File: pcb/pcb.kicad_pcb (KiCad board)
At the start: 2 copper layers, 43.2 x 132.1 mm, 49 parts, among them J1 Barrel_Jack_Switch, J2 Conn_02x05_Odd_Even, J3 Conn_02x05_Odd_Even, Q1 RQ5P010SN, Q2 IRLML6244, SW1 SW_SPST, SW2 SW_SPST, SW3 SW_SPST, U1 L7805, U2 MCP1406/07, U3 MAX6921AWI, U4 MCP7940N-xSN, U5 Pico, Y1 32.768KHZ

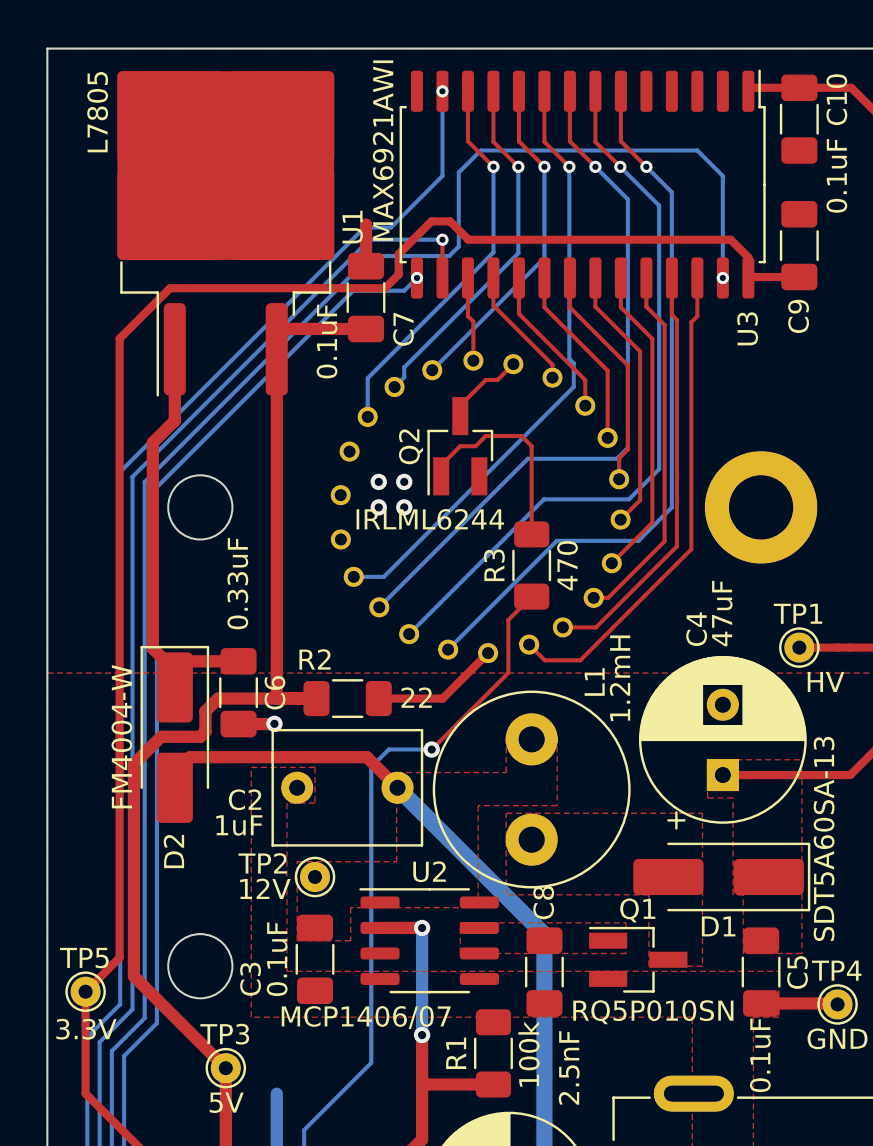
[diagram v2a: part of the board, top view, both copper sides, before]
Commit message: exchanged lm7805 for vx7805
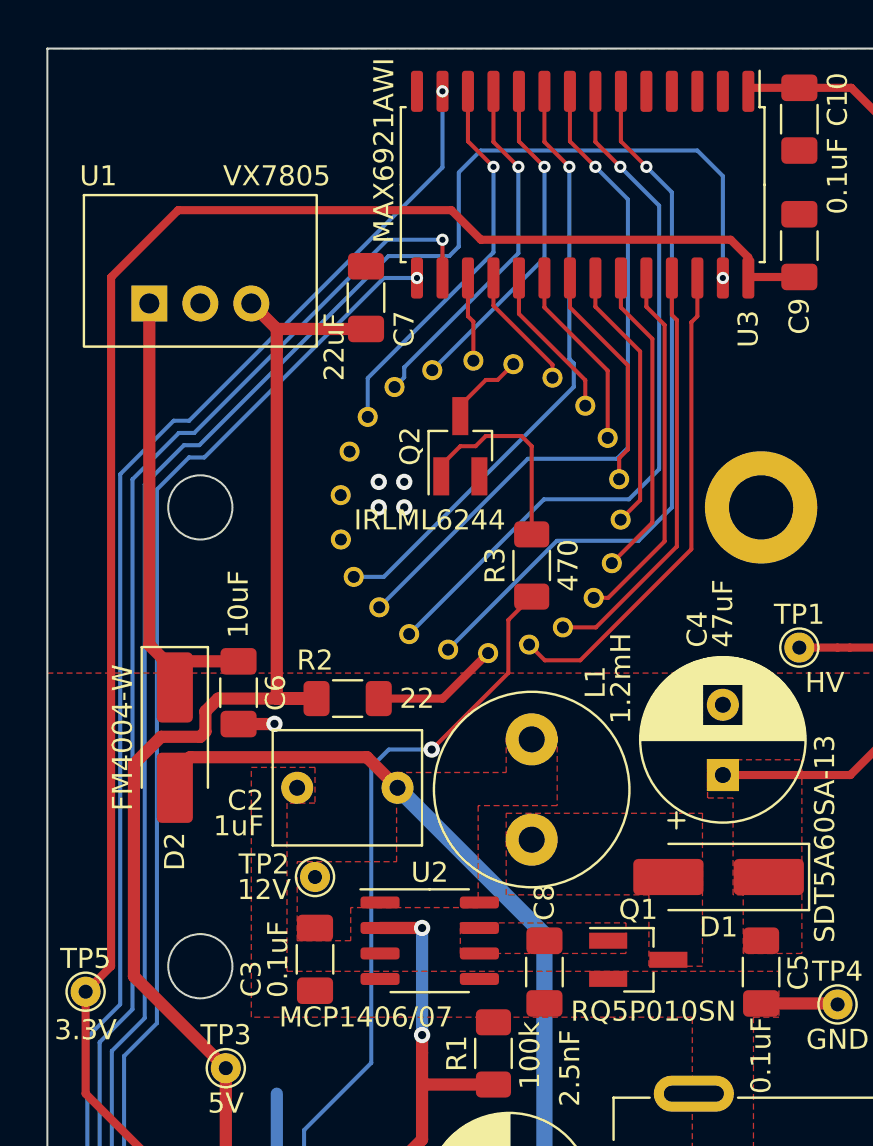
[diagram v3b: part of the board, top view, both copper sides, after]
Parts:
- C6: value 0.33uF -> 10uF
- C7: value 0.1uF -> 22uF
- F1: value Polyfuse -> 300mA
- U1: value L7805 -> VX7805; footprint Package_TO_SOT_SMD:TO-263-2 -> vfd:VX7805
- moved U1 5.52 mm to (116.8, 47.0), turned to 0 degrees
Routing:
- net GND: track 12.2 -> 10.1 mm
- net +3.3V: track 83.3 -> 85.2 mm
- net Net-(D2-K): track 22.2 -> 24.1 mm
- net +5V: track 58.6 -> 60.4 mm

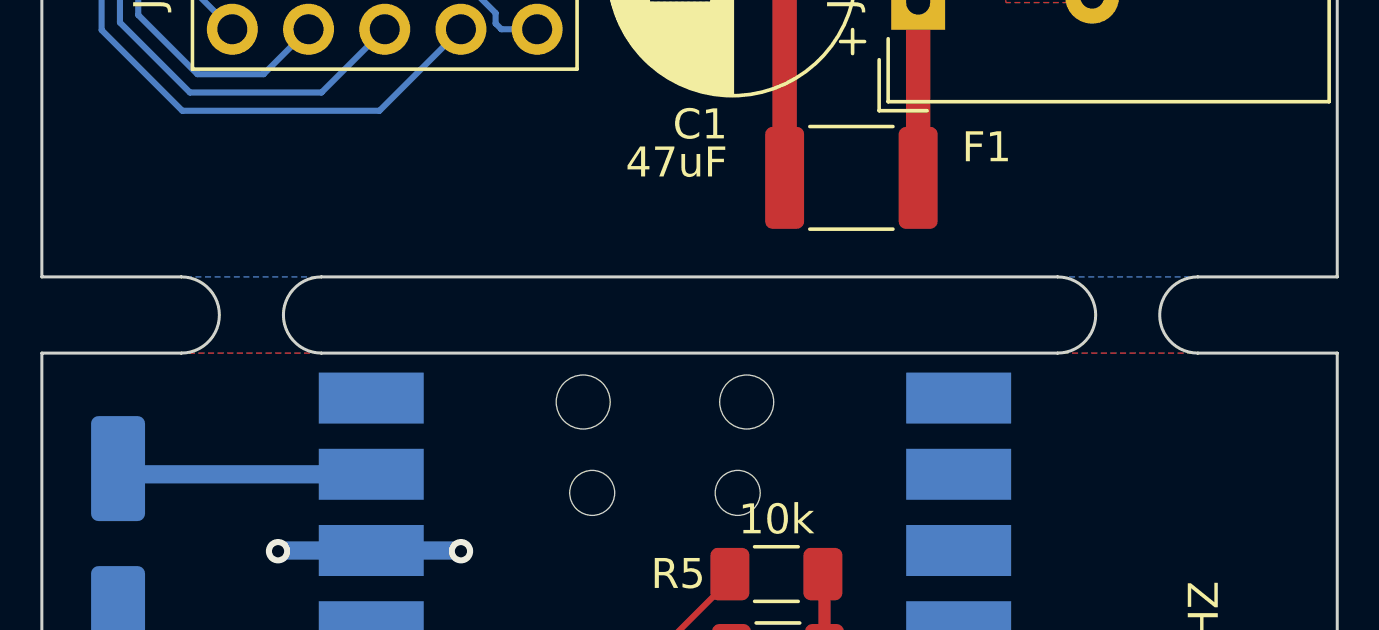
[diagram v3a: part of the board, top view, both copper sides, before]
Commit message: reintroduced mousebites
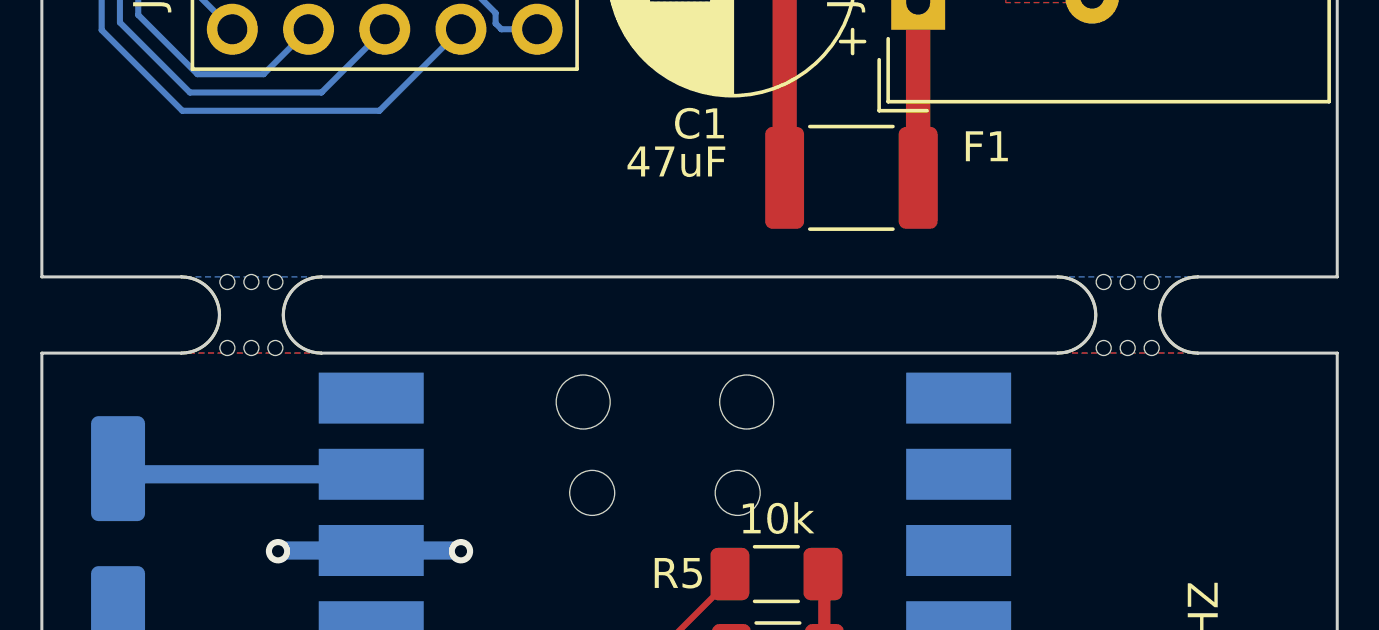
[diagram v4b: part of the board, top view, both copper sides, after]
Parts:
- added mouse-bite-2.54mm-slot: VAL**, Panelization:mouse-bite-2.54mm-slot, F.Cu at (145.4, 102.9)
- added mouse-bite-2.54mm-slot: VAL**, Panelization:mouse-bite-2.54mm-slot, F.Cu at (116.2, 102.9)
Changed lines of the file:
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@@
     )
+  )
+  (footprint "Panelization:mouse-bite-2.54mm-slot" (layer "F.Cu")
+    (at 145.415 102.87)
+    (attr through_hole)
+    (fp_text reference "mouse-bite-2.54mm-slot" (at 0 -2) (layer "F.SilkS") hide
+        (effects (font (size 1 1) (thickness 0.2)))
+    )
+    (fp_text value "VAL**" (at 0 2.1) (layer "F.SilkS") hide
+        (effects (font (size 1 1) (thickness 0.2)))
+    )
+    (fp_arc (start -2.33 -1.27) (mid -1.06 0) (end -2.33 1.27)
+      (stroke (width 0.1) (type solid)) (layer "F.SilkS"))
+    (fp_arc (start 2.33 1.27) (mid 1.06 0) (end 2.33 -1.27)
+      (stroke (width 0.1) (type solid)) (layer "F.SilkS"))
+    (fp_circle (center -2.33 0) (end -2.27 0)
+      (stroke (width 0.05) (type solid)) (fill none) (layer "Dwgs.User"))
+    (fp_circle (center 2.33 0) (end 2.33 -0.06)
+      (stroke (width 0.05) (type solid)) (fill none) (layer "Dwgs.User"))
+    (fp_line (start -2.33 0) (end -2.33 0)
+      (stroke (width 2.54) (type solid)) (layer "Eco1.User"))
+    (fp_line (start 2.33 0) (end 2.33 0)
+      (stroke (width 2.54) (type solid)) (layer "Eco1.User"))
+    (pad "" np_thru_hole circle (at -0.8 -1.1) (size 0.5 0.5) (drill 0.5) (layers "*.Cu" "*.Mask"))
+    (pad "" np_thru_hole circle (at -0.8 1.1) (size 0.5 0.5) (drill 0.5) (layers "*.Cu" "*.Mask"))
+    (pad "" np_thru_hole circle (at 0 -1.1) (size 0.5 0.5) (drill 0.5) (layers "*.Cu" "*.Mask"))
+    (pad "" np_thru_hole circle (at 0 1.1) (size 0.5 0.5) (drill 0.5) (layers "*.Cu" "*.Mask"))
+    (pad "" np_thru_hole circle (at 0.8 -1.1) (size 0.5 0.5) (drill 0.5) (layers "*.Cu" "*.Mask"))
+    (pad "" np_thru_hole circle (at 0.8 1.1) (size 0.5 0.5) (drill 0.5) (layers "*.Cu" "*.Mask"))
   )
   (footprint "TestPoint:TestPoint_THTPad_D1.5mm_Drill0.7mm" (layer "F.Cu")
@@
     )
   )
+  (footprint "Panelization:mouse-bite-2.54mm-slot" (layer "F.Cu")
+    (at 116.205 102.87)
+    (attr through_hole)
+    (fp_text reference "mouse-bite-2.54mm-slot" (at 0 -2) (layer "F.SilkS") hide
+        (effects (font (size 1 1) (thickness 0.2)))
+    )
+    (fp_text value "VAL**" (at 0 2.1) (layer "F.SilkS") hide
+        (effects (font (size 1 1) (thickness 0.2)))
+    )
+    (fp_arc (start -2.33 -1.27) (mid -1.06 0) (end -2.33 1.27)
+      (stroke (width 0.1) (type solid)) (layer "F.SilkS"))
+    (fp_arc (start 2.33 1.27) (mid 1.06 0) (end 2.33 -1.27)
+      (stroke (width 0.1) (type solid)) (layer "F.SilkS"))
+    (fp_circle (center -2.33 0) (end -2.27 0)
+      (stroke (width 0.05) (type solid)) (fill none) (layer "Dwgs.User"))
+    (fp_circle (center 2.33 0) (end 2.33 -0.06)
+      (stroke (width 0.05) (type solid)) (fill none) (layer "Dwgs.User"))
+    (fp_line (start -2.33 0) (end -2.33 0)
+      (stroke (width 2.54) (type solid)) (layer "Eco1.User"))
+    (fp_line (start 2.33 0) (end 2.33 0)
+      (stroke (width 2.54) (type solid)) (layer "Eco1.User"))
+    (pad "" np_thru_hole circle (at -0.8 -1.1) (size 0.5 0.5) (drill 0.5) (layers "*.Cu" "*.Mask"))
+    (pad "" np_thru_hole circle (at -0.8 1.1) (size 0.5 0.5) (drill 0.5) (layers "*.Cu" "*.Mask"))
+    (pad "" np_thru_hole circle (at 0 -1.1) (size 0.5 0.5) (drill 0.5) (layers "*.Cu" "*.Mask"))
+    (pad "" np_thru_hole circle (at 0 1.1) (size 0.5 0.5) (drill 0.5) (layers "*.Cu" "*.Mask"))
+    (pad "" np_thru_hole circle (at 0.8 -1.1) (size 0.5 0.5) (drill 0.5) (layers "*.Cu" "*.Mask"))
+    (pad "" np_thru_hole circle (at 0.8 1.1) (size 0.5 0.5) (drill 0.5) (layers "*.Cu" "*.Mask"))
+  )
   (footprint "TestPoint:TestPoint_THTPad_D1.5mm_Drill0.7mm" (layer "F.Cu")
